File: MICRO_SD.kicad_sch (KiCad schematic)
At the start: 9 parts, among them J12 10067099-200LF

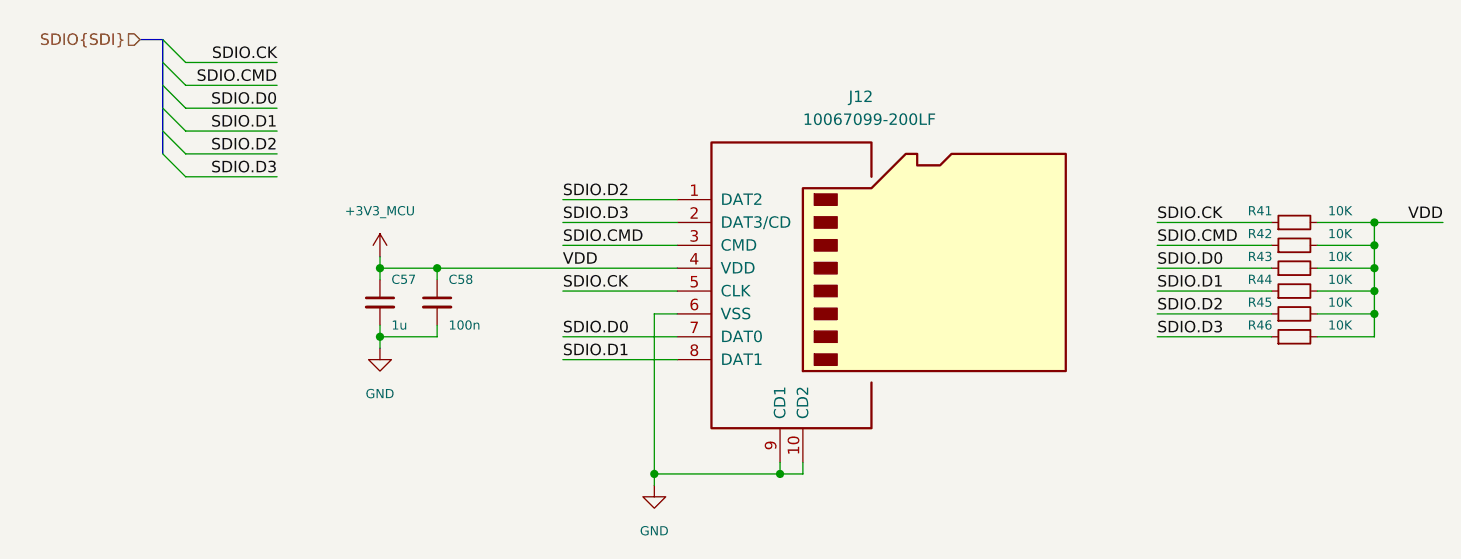
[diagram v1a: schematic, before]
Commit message: Add 22R optional SDIO clock series damping resistor
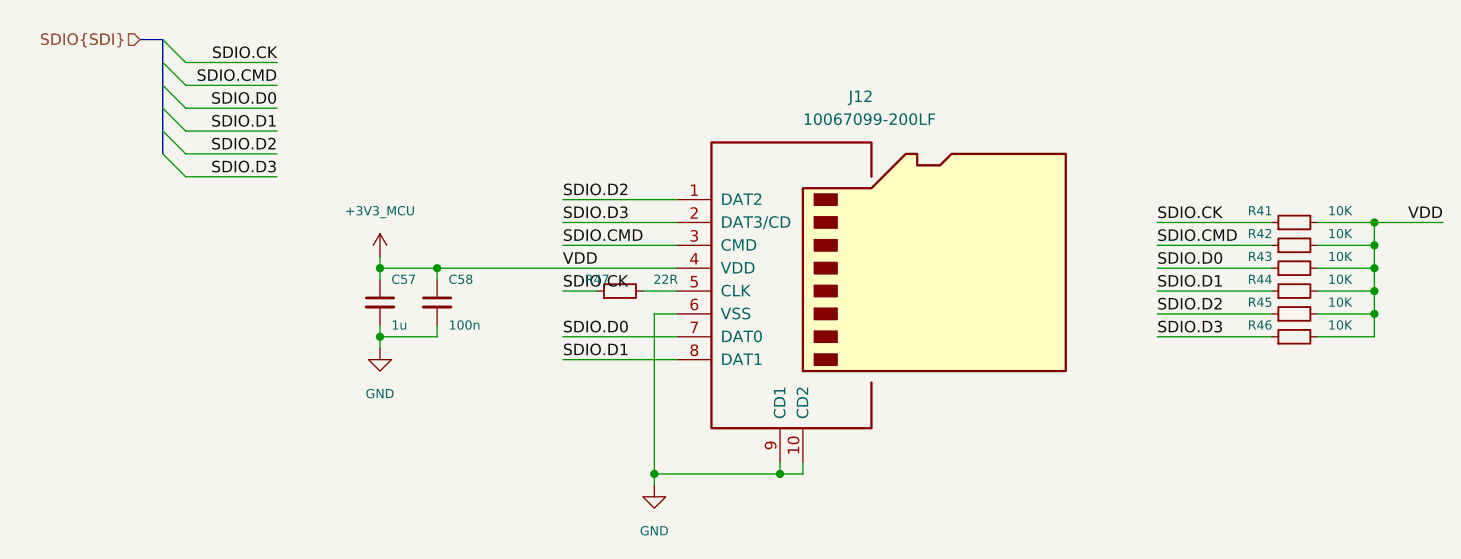
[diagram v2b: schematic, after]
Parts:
- added R47: 22R, Resistor_SMD:R_0402_1005Metric, symbol FC01_Project:MICRO_SD__R_Small
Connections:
- net SDIO.CK: now also R47.1; no longer J12.5 (CLK)
- new net: J12.5 (CLK), R47.2

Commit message: Resolve SDIO series resistor reference collision
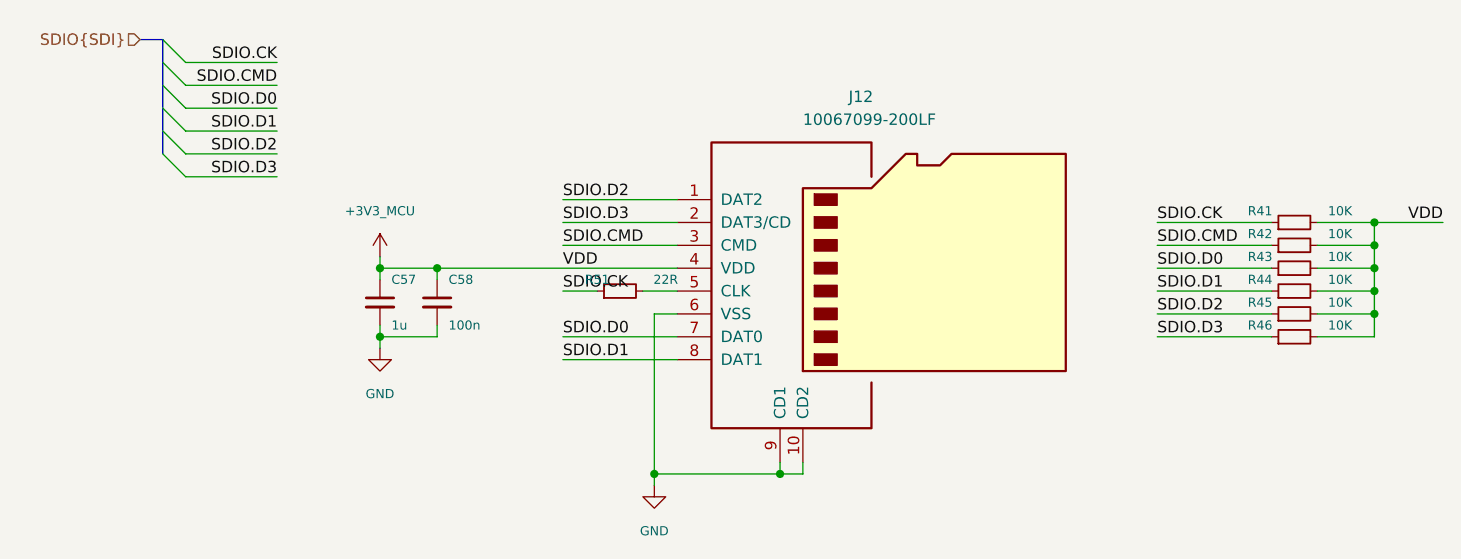
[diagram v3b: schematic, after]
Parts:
- renumbered R47 to R51
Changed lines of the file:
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@@
 		(in_pos_files yes)
 		(dnp no)
-		(property "Reference" "R47"
+		(property "Reference" "R51"
 			(at 77.47 59.69 90)
 			(show_name no)
@@
 			(project "H743_Ardupilot"
 				(path "/6b768b36-fce6-4be0-9021-6d41bddc3a70/f6fdd950-a71d-4aac-93a8-c5aad57c018b"
-					(reference "R47")
+					(reference "R51")
 					(unit 1)
 				)

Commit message: Audit FC_01 libraries nets supplier specs and placement
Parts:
- R51: Component_PDF ${KIPRJMOD}/composants/controle/RC0402FR-0722RL.pdf -> ${KIPRJMOD}/composants/pdf/R51_datasheet.pdf; Datasheet_URL https://www.mouser.com/datasheet/2/447/PYu-RC0402_51_RoHS_L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 -> https://www.yageogroup.com/component-documentation/download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; DigiKey Part Number 311-22.0LRCT-ND -> (none); DigiKey Price Qty 1 -> (none); DigiKey Status Stock positif au releve -> Offre DigiKey France non retenue ou non confirmee; DigiKey URL https://www.digikey.fr/fr/products/detail/yageo/RC0402FR-07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 -> (none); DigiKey Unit Price EUR 0.09 -> (none); DigiKey_Part_Number 311-22.0LRCT-ND -> (none); DigiKey_URL https://www.digikey.fr/fr/products/detail/yageo/RC0402FR-07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 -> (none); Footprint Audit Document fabricant Yageo RC (hébergé DigiKey): famille RC04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 -> Yageo RC0402FR-0722RL = 22 ohms, 1%, 0402 / 1005. Empreinte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; Price Checked 2026-09-27 -> (none); Price_Basis EUR HT par piece, hors port -> (none); Price_Checked 2026-09-27 -> (none); Price_Qty 1 -> (none); Stock_Checked 2026-09-27 -> (none); Stock_Units 9912210 -> (none); Supplier DigiKey France -> Non confirme; Supplier_Notes Relevé web; stock et prix variables. -> 22 ohms selon Yageo; offre France non confirmee.; Supplier_Order_Code 311-22.0LRCT-ND -> (none); Supplier_Status Stock positif au releve -> Offre France non confirmee; Supplier_URL https://www.digikey.fr/fr/products/detail/yageo/RC0402FR-07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 -> (none); Unit_Price_EUR 0.09 -> (none)
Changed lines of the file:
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@@
 			)
 		)
-		(property "Datasheet" "${KIPRJMOD}/composants/pdf/Yageo_RC.pdf"
+		(property "Datasheet" "${KIPRJMOD}/composants/pdf/R51_datasheet.pdf"
 			(at 80.01 60.96 0)
 			(hide yes)
@@
 			)
 		)
-		(property "DigiKey URL" "https://www.digikey.fr/fr/products/detail/yageo/RC0402FR-0722RL/726523"
+		(property "DigiKey URL" ""
 			(at 77.47 59.69 90)
 			(hide yes)
@@
 			)
 		)
-		(property "DigiKey Unit Price EUR" "0.09"
-			(at 77.47 59.69 90)
-			(hide yes)
-			(show_name no)
-			(do_not_autoplace no)
-			(effects
-				(font
-					(size 1.27 1.27)
-				)
-			)
-		)
-		(property "DigiKey Price Qty" "1"
-			(at 77.47 59.69 90)
-			(hide yes)
-			(show_name no)
-			(do_not_autoplace no)
-			(effects
-				(font
-					(size 1.27 1.27)
-				)
-			)
-		)
-		(property "Price Checked" "2026-09-27"
-			(at 77.47 59.69 90)
-			(hide yes)
-			(show_name no)
-			(do_not_autoplace no)
-			(effects
-				(font
-					(size 1.27 1.27)
-				)
-			)
-		)
-		(property "DigiKey Status" "Stock positif au releve"
+		(property "DigiKey Unit Price EUR" ""
+			(at 77.47 59.69 90)
+			(hide yes)
+			(show_name no)
+			(do_not_autoplace no)
+			(effects
+				(font
+					(size 1.27 1.27)
+				)
+			)
+		)
+		(property "DigiKey Price Qty" ""
+			(at 77.47 59.69 90)
+			(hide yes)
+			(show_name no)
+			(do_not_autoplace no)
+			(effects
+				(font
+					(size 1.27 1.27)
+				)
+			)
+		)
+		(property "Price Checked" ""
+			(at 77.47 59.69 90)
+			(hide yes)
+			(show_name no)
+			(do_not_autoplace no)
+			(effects
+				(font
+					(size 1.27 1.27)
+				)
+			)
+		)
+		(property "DigiKey Status" "Offre DigiKey France non retenue ou non confirmee"
 			(at 77.47 59.69 90)
 			(hide yes)
@@
 			)
 		)
-		(property "Footprint Audit" "Document fabricant Yageo RC (hébergé DigiKey): famille RC0402, corps 1.0 x 0.5 mm, deux bornes non polarisées. Empreinte KiCad 0402 conservée; suffixe de commande et valeur issus du schéma, disponibilité non recontrôlée."
+		(property "Footprint Audit" "Yageo RC0402FR-0722RL = 22 ohms, 1%, 0402 / 1005. Empreinte standard 0402; offre France non confirmee."
 			(at 77.47 59.69 90)
 			(hide yes)
@@
 			)
 		)
-		(property "DigiKey_Part_Number" "311-22.0LRCT-ND"
-			(at 0 0 0)
-			(hide yes)
-			(show_name no)
-			(do_not_autoplace no)
-			(effects
-				(font
-					(size 1.27 1.27)
-				)
-			)
-		)
-		(property "DigiKey_URL" "https://www.digikey.fr/fr/products/detail/yageo/RC0402FR-0722RL/726523"
-			(at 0 0 0)
-			(hide yes)
-			(show_name no)
-			(do_not_autoplace no)
-			(effects
-				(font
-					(size 1.27 1.27)
-				)
-			)
-		)
-		(property "Price_Checked" "2026-09-27"
-			(at 0 0 0)
-			(hide yes)
-			(show_name no)
-			(do_not_autoplace no)
-			(effects
-				(font
-					(size 1.27 1.27)
-				)
-			)
-		)
-		(property "Price_Qty" "1"
-			(at 0 0 0)
-			(hide yes)
-			(show_name no)
-			(do_not_autoplace no)
-			(effects
-				(font
-					(size 1.27 1.27)
-				)
-			)
-		)
-		(property "Stock_Units" "9912210"
-			(at 0 0 0)
-			(hide yes)
-			(show_name no)
-			(do_not_autoplace no)
-			(effects
-				(font
-					(size 1.27 1.27)
-				)
-			)
-		)
-		(property "Supplier" "DigiKey France"
-			(at 0 0 0)
-			(hide yes)
-			(show_name no)
-			(do_not_autoplace no)
-			(effects
-				(font
-					(size 1.27 1.27)
-				)
-			)
-		)
-		(property "Supplier_Order_Code" "311-22.0LRCT-ND"
-			(at 0 0 0)
-			(hide yes)
-			(show_name no)
-			(do_not_autoplace no)
-			(effects
-				(font
-					(size 1.27 1.27)
-				)
-			)
-		)
-		(property "Supplier_URL" "https://www.digikey.fr/fr/products/detail/yageo/RC0402FR-0722RL/726523"
-			(at 0 0 0)
-			(hide yes)
-			(show_name no)
-			(do_not_autoplace no)
-			(effects
-				(font
-					(size 1.27 1.27)
-				)
-			)
-		)
-		(property "Unit_Price_EUR" "0.09"
+		(property "DigiKey_Part_Number" ""
+			(at 0 0 0)
+			(hide yes)
+			(show_name no)
+			(do_not_autoplace no)
+			(effects
+				(font
+					(size 1.27 1.27)
+				)
+			)
+		)
+		(property "DigiKey_URL" ""
+			(at 0 0 0)
+			(hide yes)
+			(show_name no)
+			(do_not_autoplace no)
+			(effects
+				(font
+					(size 1.27 1.27)
+				)
+			)
+		)
+		(property "Price_Checked" ""
+			(at 0 0 0)
+			(hide yes)
+			(show_name no)
+			(do_not_autoplace no)
+			(effects
+				(font
+					(size 1.27 1.27)
+				)
+			)
+		)
+		(property "Price_Qty" ""
+			(at 0 0 0)
+			(hide yes)
+			(show_name no)
+			(do_not_autoplace no)
+			(effects
+				(font
+					(size 1.27 1.27)
+				)
+			)
+		)
+		(property "Stock_Units" ""
+			(at 0 0 0)
+			(hide yes)
+			(show_name no)
+			(do_not_autoplace no)
+			(effects
+				(font
+					(size 1.27 1.27)
+				)
+			)
+		)
+		(property "Supplier" "Non confirme"
+			(at 0 0 0)
+			(hide yes)
+			(show_name no)
+			(do_not_autoplace no)
+			(effects
+				(font
+					(size 1.27 1.27)
+				)
+			)
+		)
+		(property "Supplier_Order_Code" ""
+			(at 0 0 0)
+			(hide yes)
+			(show_name no)
+			(do_not_autoplace no)
+			(effects
+				(font
+					(size 1.27 1.27)
+				)
+			)
+		)
+		(property "Supplier_URL" ""
+			(at 0 0 0)
+			(hide yes)
+			(show_name no)
+			(do_not_autoplace no)
+			(effects
+				(font
+					(size 1.27 1.27)
+				)
+			)
+		)
+		(property "Unit_Price_EUR" ""
 			(at 0 0 0)
 			(hide yes)
@@
 			)
 		)
-		(property "Component_PDF" "${KIPRJMOD}/composants/controle/RC0402FR-0722RL.pdf"
-			(at 0 0 0)
-			(hide yes)
-			(show_name no)
-			(do_not_autoplace no)
-			(effects
-				(font
-					(size 1.27 1.27)
-				)
-			)
-		)
-		(property "Datasheet_URL" "https://www.mouser.com/datasheet/2/447/PYu-RC0402_51_RoHS_L_6_r-8721.pdf"
-			(at 0 0 0)
-			(hide yes)
-			(show_name no)
-			(do_not_autoplace no)
-			(effects
-				(font
-					(size 1.27 1.27)
-				)
-			)
-		)
-		(property "DigiKey Part Number" "311-22.0LRCT-ND"
+		(property "Component_PDF" "${KIPRJMOD}/composants/pdf/R51_datasheet.pdf"
+			(at 0 0 0)
+			(hide yes)
+			(show_name no)
+			(do_not_autoplace no)
+			(effects
+				(font
+					(size 1.27 1.27)
+				)
+			)
+		)
+		(property "Datasheet_URL" "https://www.yageogroup.com/component-documentation/download/specsheet/RC0402FR-0722RL"
+			(at 0 0 0)
+			(hide yes)
+			(show_name no)
+			(do_not_autoplace no)
+			(effects
+				(font
+					(size 1.27 1.27)
+				)
+			)
+		)
+		(property "DigiKey Part Number" ""
 			(at 0 0 0)
 			(hide yes)
@@
 			)
 		)
-		(property "Price_Basis" "EUR HT par piece, hors port"
-			(at 0 0 0)
-			(hide yes)
-			(show_name no)
-			(do_not_autoplace no)
-			(effects
-				(font
-					(size 1.27 1.27)
-				)
-			)
-		)
-		(property "Stock_Checked" "2026-09-27"
-			(at 0 0 0)
-			(hide yes)
-			(show_name no)
-			(do_not_autoplace no)
-			(effects
-				(font
-					(size 1.27 1.27)
-				)
-			)
-		)
-		(property "Supplier_Notes" "Relevé web; stock et prix variables."
-			(at 0 0 0)
-			(hide yes)
-			(show_name no)
-			(do_not_autoplace no)
-			(effects
-				(font
-					(size 1.27 1.27)
-				)
-			)
-		)
-		(property "Supplier_Status" "Stock positif au releve"
-			(at 0 0 0)
-			(hide yes)
+		(property "Price_Basis" ""
+			(at 0 0 0)
+			(hide yes)
+			(show_name no)
+			(do_not_autoplace no)
+			(effects
+				(font
+					(size 1.27 1.27)
+				)
+			)
+		)
+		(property "Stock_Checked" ""
+			(at 0 0 0)
+			(hide yes)
+			(show_name no)
+			(do_not_autoplace no)
+			(effects
+				(font
+					(size 1.27 1.27)
+				)
+			)
+		)
+		(property "Supplier_Notes" "22 ohms selon Yageo; offre France non confirmee."
+			(at 0 0 0)
+			(hide yes)
+			(show_name no)
+			(do_not_autoplace no)
+			(effects
+				(font
+					(size 1.27 1.27)
+				)
+			)
+		)
+		(property "Supplier_Status" "Offre France non confirmee"
+			(at 0 0 0)
+			(hide yes)

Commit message: Correct ERC pin models and power connectivity
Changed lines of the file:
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@@
 		)
 	)
-	(label "VDD"
+	(label "+3V3_MCU"
 		(at 73.66 58.42 0)
 		(effects
@@
 		)
 	)
-	(label "VDD"
+	(label "+3V3_MCU"
 		(at 171.45 53.34 180)
 		(effects

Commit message: pos down
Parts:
- removed R51: 22R, Resistor_SMD:R_0402_1005Metric, symbol FC01_Project:MICRO_SD__R_Small
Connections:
- net SDIO.CK: now also J12.5 (CLK)
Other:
- moved on the sheet: R41, R42, R43, R44, R45, R46
